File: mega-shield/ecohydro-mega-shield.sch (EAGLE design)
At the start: 99 parts, among them IC1 MCP1700-330, IC2 DS1306E, IC3 74HC125D, IC4 AP3211KTR, Q1 IRLM5103, Q10 PBSS4021NT,215, Q11 PBSS4021NT,215, Q12 PBSS4021NT,215, Q13 PBSS4021NT,215, Q14 PBSS4021NT,215, Q15 PBSS4021NT,215, Q16 PBSS4021NT,215, Q17 IRLM5103, Q18 IRLM5103, Q19 IRLM5103, Q2 IRLM5103, Q20 PBSS4021NT,215, Q21 PBSS4021NT,215, Q22 PBSS4021NT,215, Q3 IRLM5103, Q4 IRLM5103, Q5 IRLM5103, Q6 IRLM5103, Q7 IRLM5103, Q8 IRLM5103, Q9 PBSS4021NT,215, U1 ARDUINO-MEGA, Y1 32.768KHZ

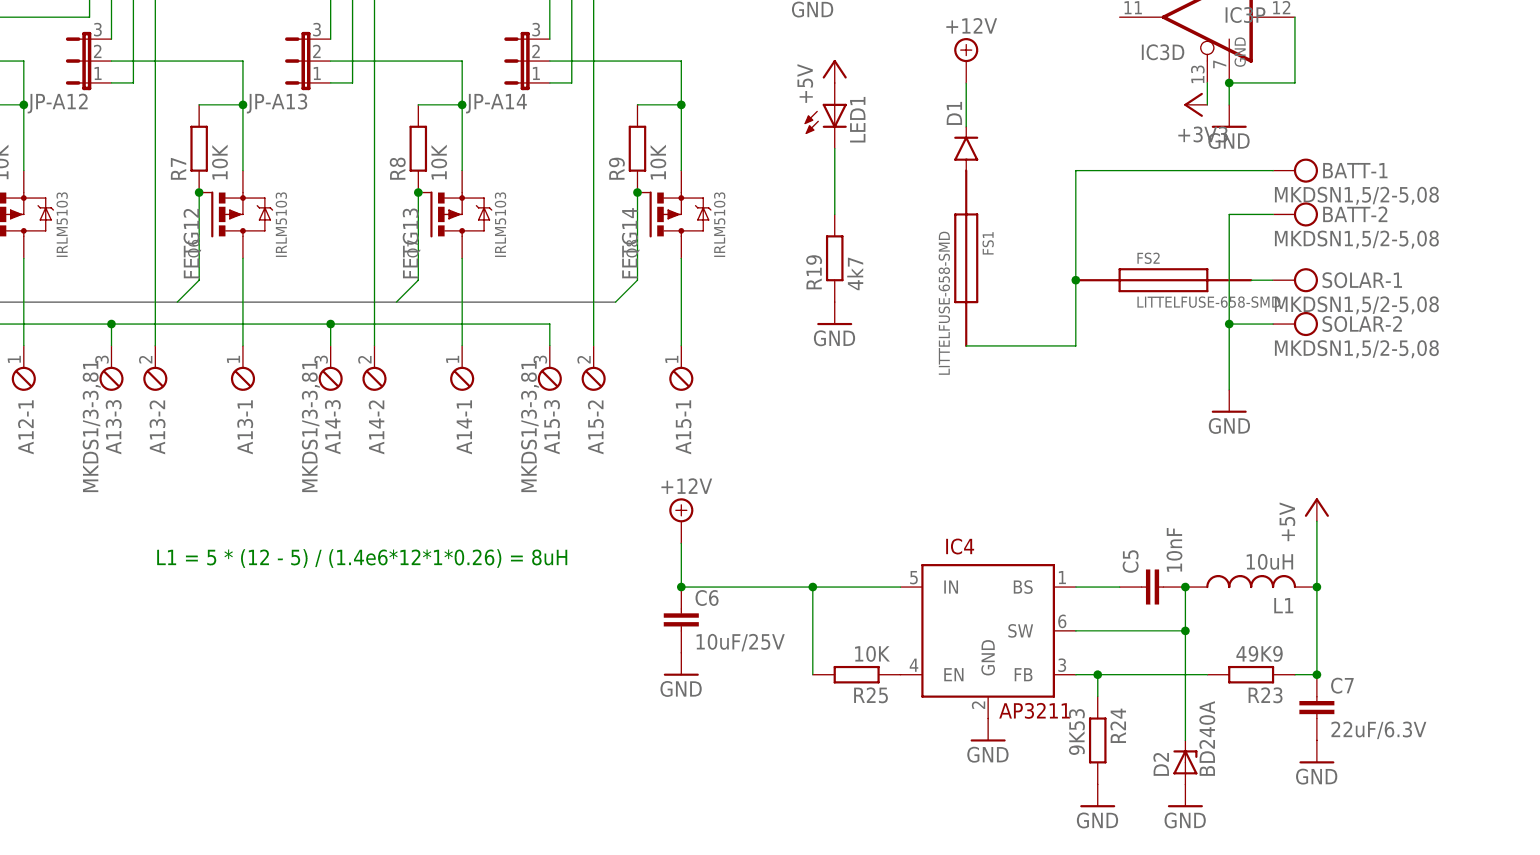
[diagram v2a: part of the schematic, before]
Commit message: Rev 1.4 - Reduced board size by 2mm to fit 10x10 economy pcb mfg
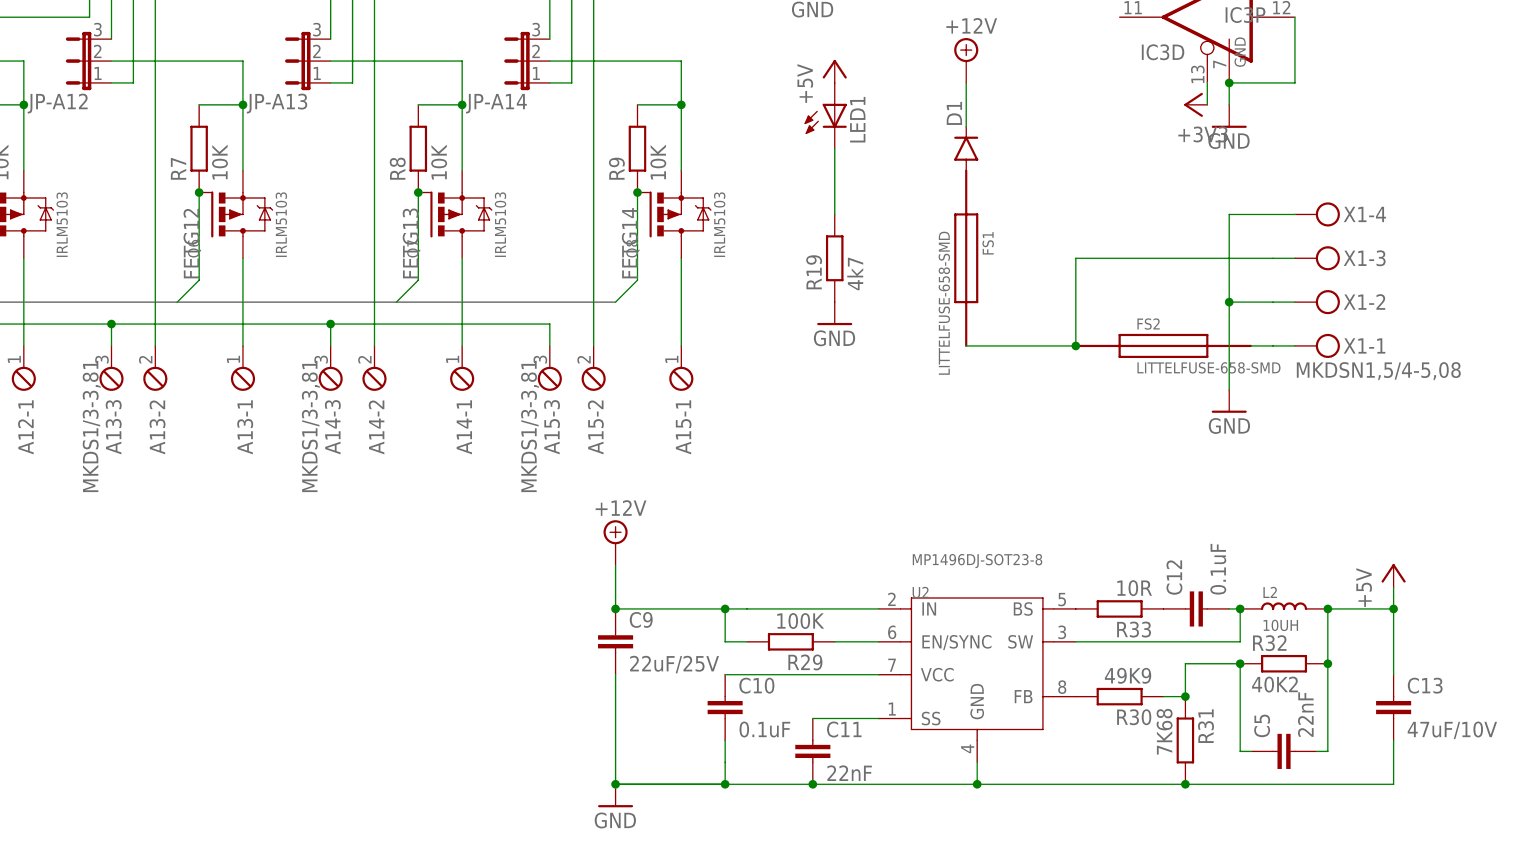
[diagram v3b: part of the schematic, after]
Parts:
- removed BATT, SOLAR: MKDSN1,5/2-5,08, mechanical:MKDSN1,5/2-5,08
- removed C6: 10uF/25V, rcl:C-EUC0805K
- removed C7: 22uF/6.3V, rcl:C-EUC0805K
- removed D2: BD240A, semiconductors:ZENER-DIODE-DO214AC
- removed IC4: AP3211KTR, semiconductors:AP3211KTR
- removed L1: 10uH, passives:L-USSRN6028N
- removed R23: 49K9, rcl:R-EU_M0805
- removed R24: 9K53, rcl:R-EU_M0805
- removed R25: 10K, rcl:R-EU_M0805
- added C10, C12: 0.1uF, rcl:C-EUC0805K
- added C11: 22nF, rcl:C-EUC0805K
- added C13: 47uF/10V, rcl:C-EUC0805K
- added C9: 22uF/25V, rcl:C-EUC0805K
- added L2: 10UH, Seeed-Inductor-2016:SMD-INDUCTOR-10UH-20%(2P-6X6MM)'0630'
- added R29: 100K, rcl:R-EU_M0805
- added R30: 49K9, rcl:R-EU_M0805
- added R31: 7K68, rcl:R-EU_M0805
- added R32: 40K2, rcl:R-EU_M0805
- added R33: 10R, rcl:R-EU_M0805
- added U2: MP1496DJ-SOT23-8, Seeed-IC-2016:PMIC-MP1496DJ(SOT23-8)
- added X1: MKDSN1,5/4-5,08, mechanical:MKDSN1,5/4-5,08
- C5: value 10nF -> 22nF; DIGIKEY 490-1664-1-ND -> (none)
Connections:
- removed net N$62: C5.1, IC4.BS
- removed net N$63: C5.2, D2.C, IC4.SW, L1.1
- removed net N$64: IC4.EN, R25.1
- removed net N$66: IC4.FB, R23.2, R24.1
- new net N$72: C10.1, U2.VCC
- new net N$74: R29.1, U2.EN/SYNC
- new net N$75: C11.1, U2.SS
- new net N$78: R30.2, U2.FB
- new net N$79: C5.1, R30.1, R31.1, R32.1
- new net N$80: C12.2, L2.1, U2.SW
- new net N$82: R33.2, U2.BS
- new net N$83: C12.1, R33.1
- net +12V: now also C9.1, R29.2, U2.IN; no longer C6.1, IC4.IN, R25.2
- net +5V: now also C13.1, C5.2, L2.2, R32.2; no longer C7.1, L1.2, R23.1
- net GND: now also C10.2, C11.2, C13.2, C9.2, R31.2, U2.GND, X1-2.KL, X1-4.KL; no longer BATT-2.KL, C6.2, C7.2, D2.A, IC4.GND, R24.2, SOLAR-2.KL
- net N$44: now also X1-3.KL; no longer BATT-1.KL
- net N$45: now also X1-1.KL; no longer SOLAR-1.KL
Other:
- note removed: "L1 = 5 * (12 - 5) / (1.4e6*12*1*0.26) = 8uH"
- moved on the sheet: C5, FS2

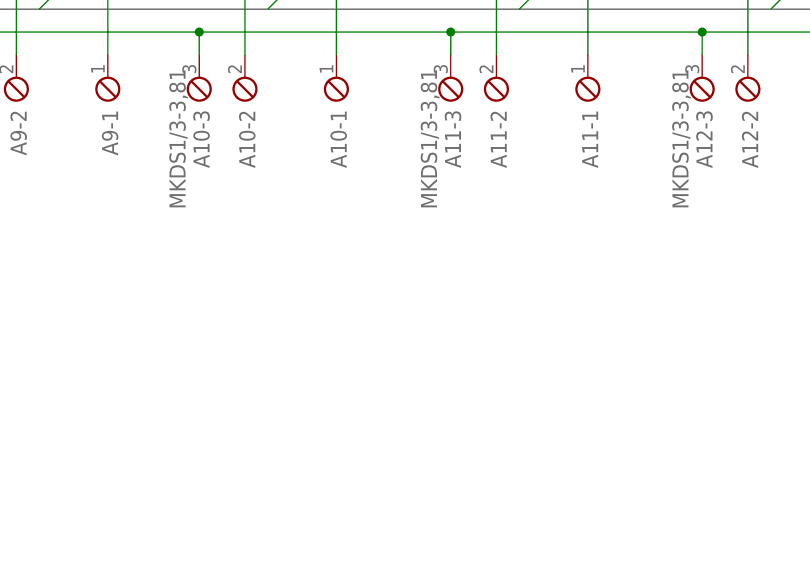
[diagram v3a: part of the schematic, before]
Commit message: Rev 1.5 - Add fiducials
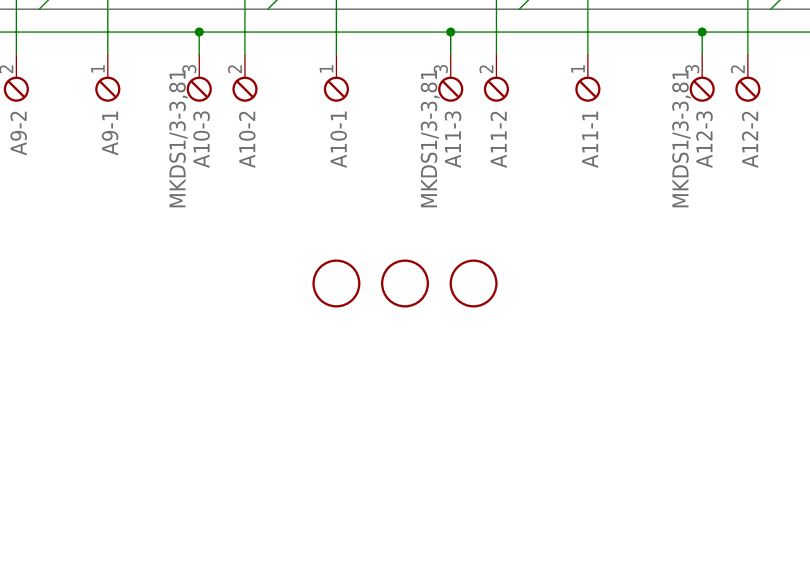
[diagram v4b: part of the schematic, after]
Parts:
- added U$2, U$3, U$4: FIDUCIAL, adafruit:FIDUCIAL
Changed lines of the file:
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@@
 <part name="C5" library="rcl" deviceset="C-EU" device="C0805K" value="22nF"/>
 <part name="X1" library="mechanical" deviceset="MKDSN1,5/4-5,08" device=""/>
+<part name="U$2" library="adafruit" deviceset="FIDUCIAL" device=""/>
+<part name="U$3" library="adafruit" deviceset="FIDUCIAL" device=""/>
+<part name="U$4" library="adafruit" deviceset="FIDUCIAL" device=""/>
 </parts>
 <sheets>
@@
 <instance part="X1" gate="-3" x="180.34" y="7.62"/>
 <instance part="X1" gate="-4" x="180.34" y="12.7"/>
+<instance part="U$2" gate="G$1" x="-25.4" y="-27.94"/>
+<instance part="U$3" gate="G$1" x="-17.78" y="-27.94"/>
+<instance part="U$4" gate="G$1" x="-10.16" y="-27.94"/>
 </instances>
 <busses>

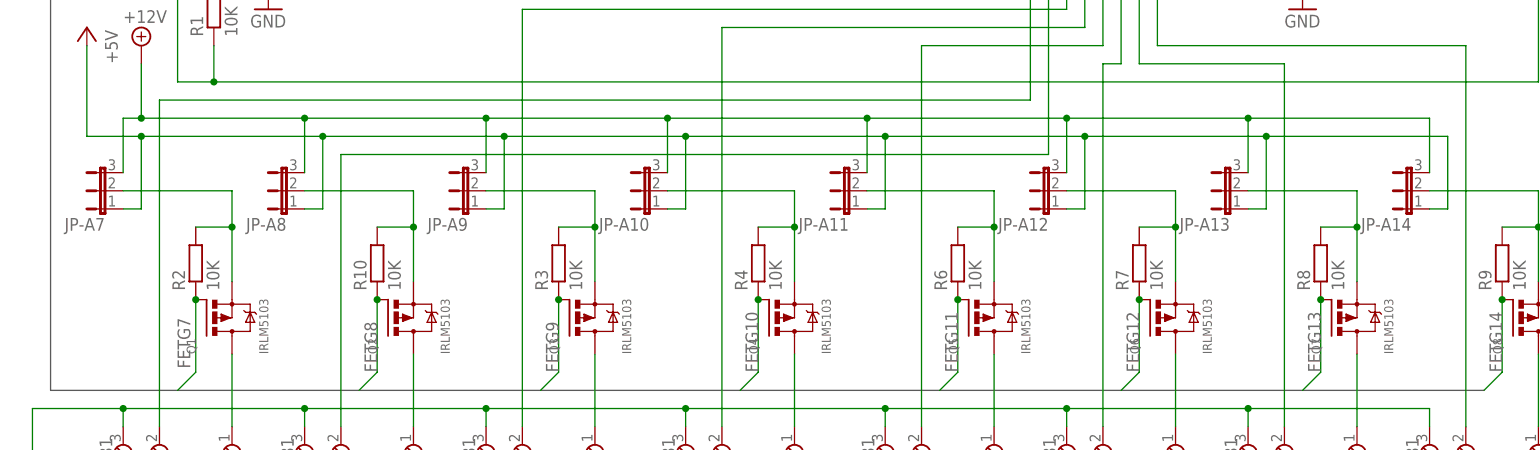
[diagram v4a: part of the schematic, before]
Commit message: Fix designators on power select jumpers
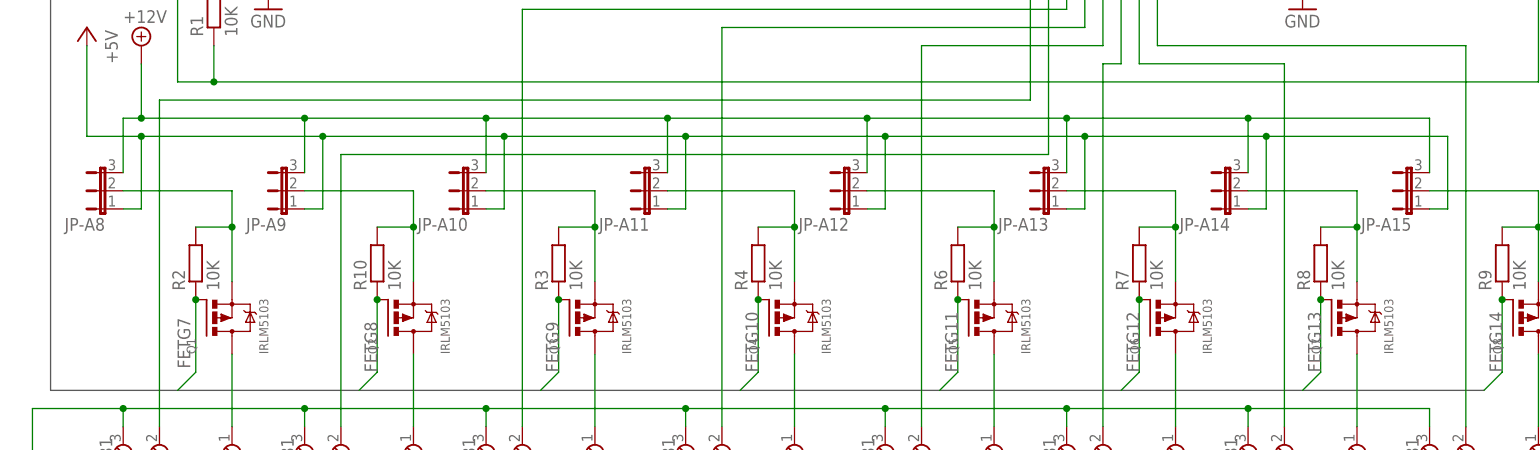
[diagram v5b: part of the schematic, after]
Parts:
- removed JP-A7: (no value), jumper:JP2E
- added JP-A15: (no value), jumper:JP2E
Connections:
- net +12V: now also JP-A15.3; no longer JP-A7.3
- net +5V: now also JP-A15.1; no longer JP-A7.1
- net N$16: now also JP-A8.2; no longer JP-A7.2
- net N$19: now also JP-A10.2; no longer JP-A9.2
- net N$21: now also JP-A15.2; no longer JP-A14.2
- net N$22: now also JP-A14.2; no longer JP-A13.2
- net N$23: now also JP-A13.2; no longer JP-A12.2
- net N$24: now also JP-A12.2; no longer JP-A11.2
- net N$25: now also JP-A11.2; no longer JP-A10.2
- net N$26: now also JP-A9.2; no longer JP-A8.2
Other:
- moved on the sheet: JP-A10, JP-A11, JP-A12, JP-A13, JP-A14, JP-A8, JP-A9
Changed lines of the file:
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@@
 <part name="A15" library="con-phoenix-381" deviceset="MKDS1/3-3,81" device=""/>
 <part name="GND3" library="supply1" deviceset="GND" device=""/>
-<part name="JP-A7" library="jumper" deviceset="JP2E" device=""/>
 <part name="JP-A8" library="jumper" deviceset="JP2E" device=""/>
 <part name="JP-A9" library="jumper" deviceset="JP2E" device=""/>
@@
 <part name="JP-A13" library="jumper" deviceset="JP2E" device=""/>
 <part name="JP-A14" library="jumper" deviceset="JP2E" device=""/>
+<part name="JP-A15" library="jumper" deviceset="JP2E" device=""/>
 <part name="SUPPLY1" library="supply2" deviceset="+12V" device=""/>
 <part name="P+6" library="supply1" deviceset="+5V" device=""/>
@@
 <instance part="A15" gate="-3" x="91.44" y="-5.08" rot="R270"/>
 <instance part="GND3" gate="1" x="-104.14" y="-10.16"/>
-<instance part="JP-A7" gate="1" x="-93.98" y="30.48" rot="R90"/>
-<instance part="JP-A8" gate="1" x="-68.58" y="30.48" rot="R90"/>
-<instance part="JP-A9" gate="1" x="-43.18" y="30.48" rot="R90"/>
-<instance part="JP-A10" gate="1" x="-17.78" y="30.48" rot="R90"/>
-<instance part="JP-A11" gate="1" x="10.16" y="30.48" rot="R90"/>
-<instance part="JP-A12" gate="1" x="38.1" y="30.48" rot="R90"/>
-<instance part="JP-A13" gate="1" x="63.5" y="30.48" rot="R90"/>
-<instance part="JP-A14" gate="1" x="88.9" y="30.48" rot="R90"/>
+<instance part="JP-A8" gate="1" x="-93.98" y="30.48" rot="R90"/>
+<instance part="JP-A9" gate="1" x="-68.58" y="30.48" rot="R90"/>
+<instance part="JP-A10" gate="1" x="-43.18" y="30.48" rot="R90"/>
+<instance part="JP-A11" gate="1" x="-17.78" y="30.48" rot="R90"/>
+<instance part="JP-A12" gate="1" x="10.16" y="30.48" rot="R90"/>
+<instance part="JP-A13" gate="1" x="38.1" y="30.48" rot="R90"/>
+<instance part="JP-A14" gate="1" x="63.5" y="30.48" rot="R90"/>
+<instance part="JP-A15" gate="1" x="88.9" y="30.48" rot="R90"/>
 <instance part="SUPPLY1" gate="+12V" x="-88.9" y="50.8"/>
 <instance part="P+6" gate="1" x="-96.52" y="53.34" rot="MR0"/>
@@
 <wire x1="68.58" y1="38.1" x2="93.98" y2="38.1" width="0.1524" layer="91"/>
 <wire x1="93.98" y1="38.1" x2="93.98" y2="27.94" width="0.1524" layer="91"/>
-<pinref part="JP-A14" gate="1" pin="1"/>
+<pinref part="JP-A15" gate="1" pin="1"/>
 <wire x1="93.98" y1="27.94" x2="91.44" y2="27.94" width="0.1524" layer="91"/>
-<pinref part="JP-A7" gate="1" pin="1"/>
+<pinref part="JP-A8" gate="1" pin="1"/>
 <wire x1="-91.44" y1="27.94" x2="-88.9" y2="27.94" width="0.1524" layer="91"/>
 <wire x1="-88.9" y1="27.94" x2="-88.9" y2="38.1" width="0.1524" layer="91"/>
-<pinref part="JP-A8" gate="1" pin="1"/>
+<pinref part="JP-A9" gate="1" pin="1"/>
 <wire x1="-66.04" y1="27.94" x2="-63.5" y2="27.94" width="0.1524" layer="91"/>
 <wire x1="-63.5" y1="27.94" x2="-63.5" y2="38.1" width="0.1524" layer="91"/>
-<pinref part="JP-A9" gate="1" pin="1"/>
+<pinref part="JP-A10" gate="1" pin="1"/>
 <wire x1="-40.64" y1="27.94" x2="-38.1" y2="27.94" width="0.1524" layer="91"/>
 <wire x1="-38.1" y1="27.94" x2="-38.1" y2="38.1" width="0.1524" layer="91"/>
-<pinref part="JP-A10" gate="1" pin="1"/>
+<pinref part="JP-A11" gate="1" pin="1"/>
 <wire x1="-15.24" y1="27.94" x2="-12.7" y2="27.94" width="0.1524" layer="91"/>
 <wire x1="-12.7" y1="27.94" x2="-12.7" y2="38.1" width="0.1524" layer="91"/>
-<pinref part="JP-A11" gate="1" pin="1"/>
+<pinref part="JP-A12" gate="1" pin="1"/>
 <wire x1="12.7" y1="27.94" x2="15.24" y2="27.94" width="0.1524" layer="91"/>
 <wire x1="15.24" y1="27.94" x2="15.24" y2="38.1" width="0.1524" layer="91"/>
-<pinref part="JP-A12" gate="1" pin="1"/>
+<pinref part="JP-A13" gate="1" pin="1"/>
 <wire x1="40.64" y1="27.94" x2="43.18" y2="27.94" width="0.1524" layer="91"/>
 <wire x1="43.18" y1="27.94" x2="43.18" y2="38.1" width="0.1524" layer="91"/>
-<pinref part="JP-A13" gate="1" pin="1"/>
+<pinref part="JP-A14" gate="1" pin="1"/>
 <wire x1="66.04" y1="27.94" x2="68.58" y2="27.94" width="0.1524" layer="91"/>
 <wire x1="68.58" y1="27.94" x2="68.58" y2="38.1" width="0.1524" layer="91"/>
@@
 <wire x1="66.04" y1="40.64" x2="91.44" y2="40.64" width="0.1524" layer="91"/>
 <wire x1="91.44" y1="40.64" x2="91.44" y2="33.02" width="0.1524" layer="91"/>
+<pinref part="JP-A15" gate="1" pin="3"/>
 <pinref part="JP-A14" gate="1" pin="3"/>
+<wire x1="66.04" y1="33.02" x2="66.04" y2="40.64" width="0.1524" layer="91"/>
 <pinref part="JP-A13" gate="1" pin="3"/>
-<wire x1="66.04" y1="33.02" x2="66.04" y2="40.64" width="0.1524" layer="91"/>
+<wire x1="40.64" y1="33.02" x2="40.64" y2="40.64" width="0.1524" layer="91"/>
 <pinref part="JP-A12" gate="1" pin="3"/>
-<wire x1="40.64" y1="33.02" x2="40.64" y2="40.64" width="0.1524" layer="91"/>
+<wire x1="12.7" y1="33.02" x2="12.7" y2="40.64" width="0.1524" layer="91"/>
 <pinref part="JP-A11" gate="1" pin="3"/>
-<wire x1="12.7" y1="33.02" x2="12.7" y2="40.64" width="0.1524" layer="91"/>
+<wire x1="-15.24" y1="33.02" x2="-15.24" y2="40.64" width="0.1524" layer="91"/>
 <pinref part="JP-A10" gate="1" pin="3"/>
-<wire x1="-15.24" y1="33.02" x2="-15.24" y2="40.64" width="0.1524" layer="91"/>
+<wire x1="-40.64" y1="33.02" x2="-40.64" y2="40.64" width="0.1524" layer="91"/>
 <pinref part="JP-A9" gate="1" pin="3"/>
-<wire x1="-40.64" y1="33.02" x2="-40.64" y2="40.64" width="0.1524" layer="91"/>
+<wire x1="-66.04" y1="33.02" x2="-66.04" y2="40.64" width="0.1524" layer="91"/>
 <pinref part="JP-A8" gate="1" pin="3"/>
-<wire x1="-66.04" y1="33.02" x2="-66.04" y2="40.64" width="0.1524" layer="91"/>
-<pinref part="JP-A7" gate="1" pin="3"/>
 <wire x1="-91.44" y1="33.02" x2="-91.44" y2="40.64" width="0.1524" layer="91"/>
 <junction x="-66.04" y="40.64"/>
@@
 <pinref part="Q1" gate="G$1" pin="S"/>
 <wire x1="-76.2" y1="17.78" x2="-76.2" y2="25.4" width="0.1524" layer="91"/>
-<pinref part="JP-A7" gate="1" pin="2"/>
+<pinref part="JP-A8" gate="1" pin="2"/>
 <wire x1="-76.2" y1="25.4" x2="-76.2" y2="30.48" width="0.1524" layer="91"/>
 <wire x1="-76.2" y1="30.48" x2="-91.44" y2="30.48" width="0.1524" layer="91"/>
@@
 <pinref part="Q3" gate="G$1" pin="S"/>
 <wire x1="-25.4" y1="17.78" x2="-25.4" y2="25.4" width="0.1524" layer="91"/>
-<pinref part="JP-A9" gate="1" pin="2"/>
+<pinref part="JP-A10" gate="1" pin="2"/>
 <wire x1="-25.4" y1="25.4" x2="-25.4" y2="30.48" width="0.1524" layer="91"/>
 <wire x1="-25.4" y1="30.48" x2="-40.64" y2="30.48" width="0.1524" layer="91"/>
@@
 <net name="N$21" class="0">
 <segment>
-<pinref part="JP-A14" gate="1" pin="2"/>
+<pinref part="JP-A15" gate="1" pin="2"/>
 <wire x1="91.44" y1="30.48" x2="106.68" y2="30.48" width="0.1524" layer="91"/>
 <pinref part="Q8" gate="G$1" pin="S"/>
@@
 <net name="N$22" class="0">
 <segment>
-<pinref part="JP-A13" gate="1" pin="2"/>
+<pinref part="JP-A14" gate="1" pin="2"/>
 <wire x1="66.04" y1="30.48" x2="81.28" y2="30.48" width="0.1524" layer="91"/>
 <pinref part="Q7" gate="G$1" pin="S"/>
@@
 <pinref part="Q6" gate="G$1" pin="S"/>
 <wire x1="55.88" y1="17.78" x2="55.88" y2="25.4" width="0.1524" layer="91"/>
-<pinref part="JP-A12" gate="1" pin="2"/>
+<pinref part="JP-A13" gate="1" pin="2"/>
 <wire x1="55.88" y1="25.4" x2="55.88" y2="30.48" width="0.1524" layer="91"/>
 <wire x1="55.88" y1="30.48" x2="40.64" y2="30.48" width="0.1524" layer="91"/>
@@
 <pinref part="Q5" gate="G$1" pin="S"/>
 <wire x1="30.48" y1="17.78" x2="30.48" y2="25.4" width="0.1524" layer="91"/>
-<pinref part="JP-A11" gate="1" pin="2"/>
+<pinref part="JP-A12" gate="1" pin="2"/>
 <wire x1="30.48" y1="25.4" x2="30.48" y2="30.48" width="0.1524" layer="91"/>
 <wire x1="30.48" y1="30.48" x2="12.7" y2="30.48" width="0.1524" layer="91"/>
@@
 <wire x1="2.54" y1="17.78" x2="2.54" y2="25.4" width="0.1524" layer="91"/>
 <wire x1="2.54" y1="25.4" x2="2.54" y2="30.48" width="0.1524" layer="91"/>
-<pinref part="JP-A10" gate="1" pin="2"/>
+<pinref part="JP-A11" gate="1" pin="2"/>
 <wire x1="2.54" y1="30.48" x2="-15.24" y2="30.48" width="0.1524" layer="91"/>
 <pinref part="R4" gate="G$1" pin="2"/>
@@
 <wire x1="-50.8" y1="17.78" x2="-50.8" y2="25.4" width="0.1524" layer="91"/>
 <wire x1="-50.8" y1="25.4" x2="-50.8" y2="30.48" width="0.1524" layer="91"/>
-<pinref part="JP-A8" gate="1" pin="2"/>
+<pinref part="JP-A9" gate="1" pin="2"/>
 <wire x1="-50.8" y1="30.48" x2="-66.04" y2="30.48" width="0.1524" layer="91"/>
 <pinref part="R10" gate="G$1" pin="2"/>
